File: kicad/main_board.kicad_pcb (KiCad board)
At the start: 2 copper layers, 42 x 67 mm, 55 parts, among them J1 Conn_01x07, J2 Conn_01x07, J3 Conn_01x07, J4 Conn_01x07, J5 Conn_01x07, J6 TYPE-C-31-M-12, J7 TYPE-C-31-M-12, Q1 Q_NPN_BEC, Q2 Q_NPN_BEC, Q3 Q_NPN_BEC, Q4 Q_NPN_BEC, Q5 Q_NPN_BEC, SW1 Reset, SW2 Boot, U1 esp32-s2-wroom, U2 XC6220B331MR, U3 USBLC6-2SC6, U4 USBLC6-2SC6, U5 LMV324, U6 LMV324

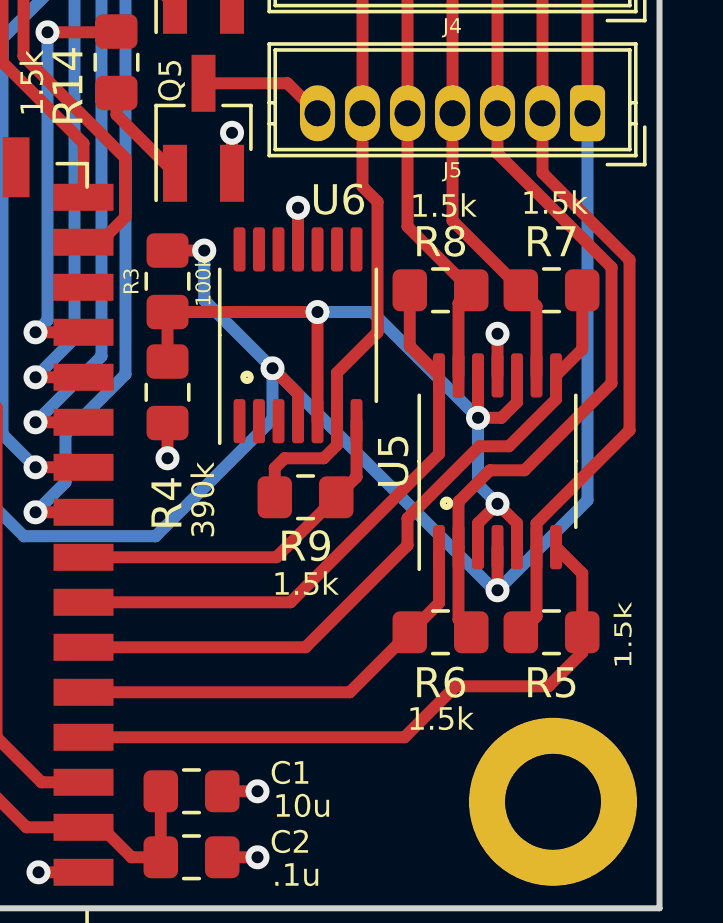
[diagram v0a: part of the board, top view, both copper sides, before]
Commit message: Update the various sensitivity-related resistor values
This updates the transimpedance amplifier resistors to 2k, and adjusts
the LED drive resistors to an appropriate level, from empirical testing.
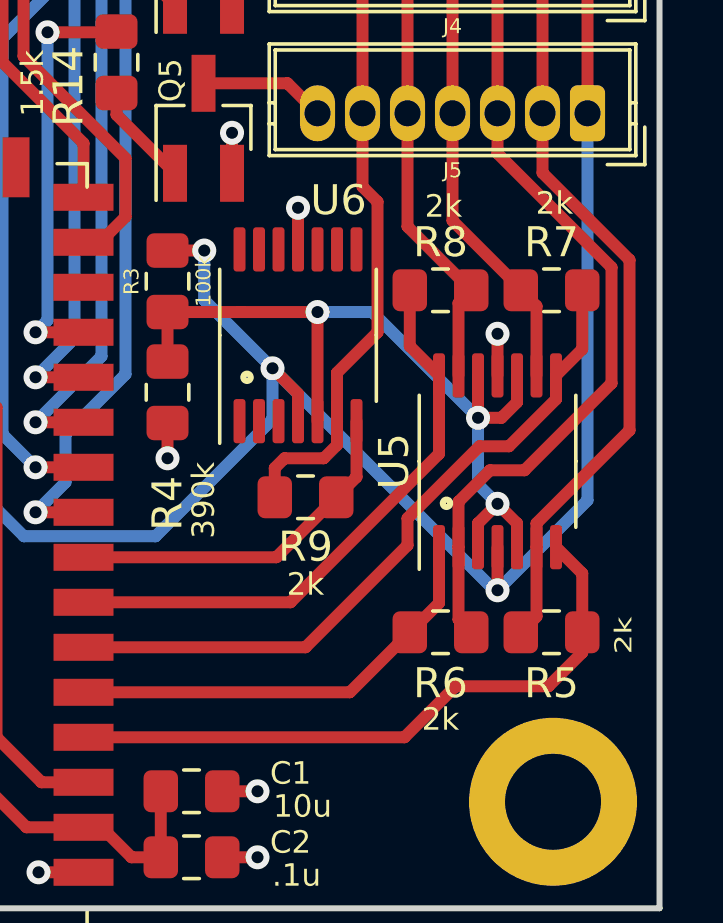
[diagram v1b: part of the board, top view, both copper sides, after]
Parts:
- R5, R6, R7, R8, R9: value 1.5k -> 2k
- U1: value esp32-s2-wroom -> esp32-s2-wrover

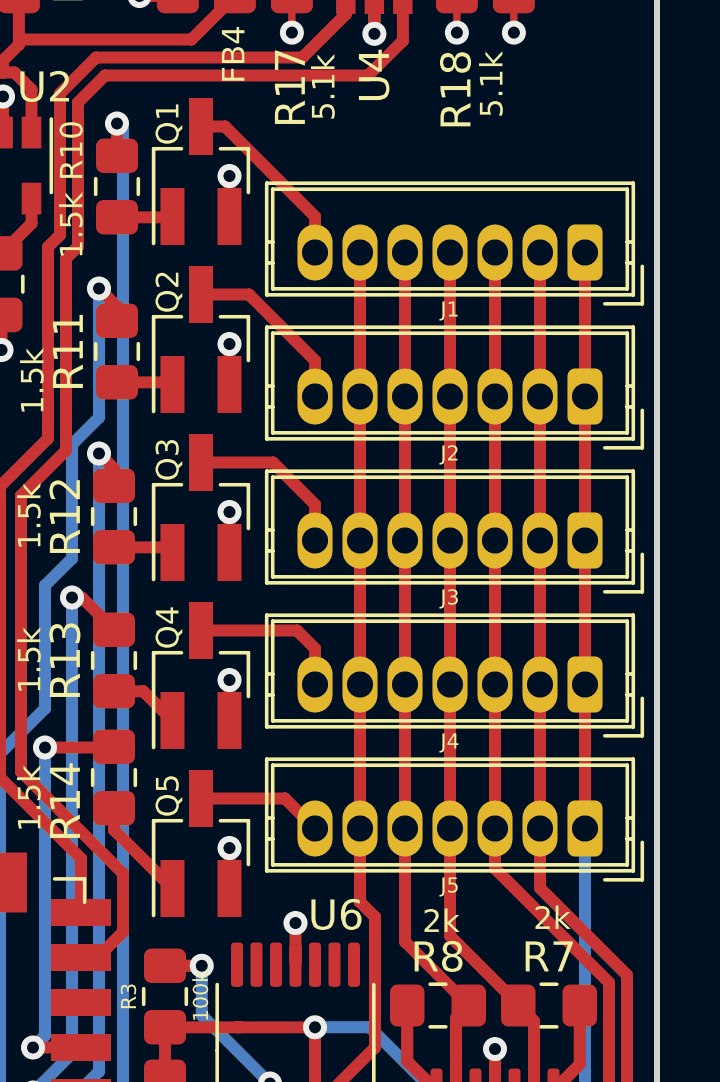
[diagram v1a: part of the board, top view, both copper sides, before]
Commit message: Reverse the cluster connectors on the main board
This reverses the connectors, so the orientation is correct for a normally
wired cable.
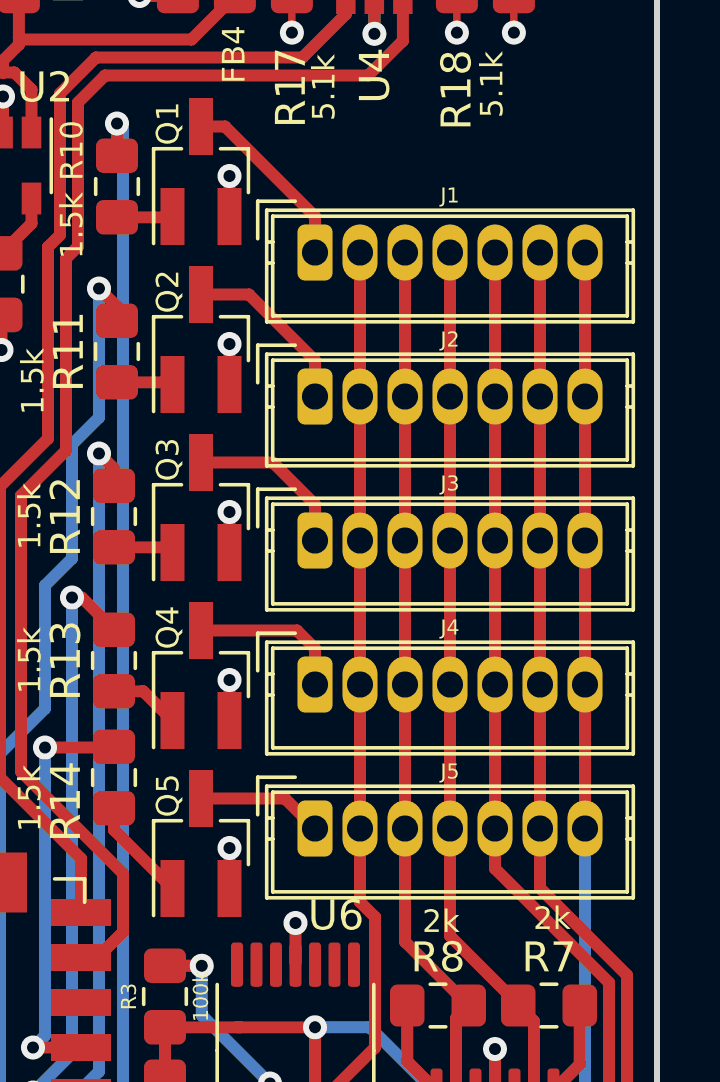
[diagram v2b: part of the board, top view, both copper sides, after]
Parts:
- U1: value esp32-s2-wrover -> esp32-s2-wroom
- moved J1 9.00 mm to (180.6, 54.3), turned to 0 degrees
- moved J2 9.00 mm to (180.6, 59.1), turned to 0 degrees
- moved J3 9.00 mm to (180.6, 63.9), turned to 0 degrees
- moved J4 9.00 mm to (180.6, 68.7), turned to 0 degrees
- moved J5 9.00 mm to (180.6, 73.5), turned to 0 degrees
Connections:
- J1 pad 1: +3V3 -> Net-(J1-Pad1)
- J1 pad 2: /COL1 -> /COL5
- J1 pad 3: /COL2 -> /COL4
- J1 pad 5: /COL4 -> /COL2
- J1 pad 6: /COL5 -> /COL1
- J1 pad 7: Net-(J1-Pad7) -> +3V3
- J2 pad 1: +3V3 -> Net-(J2-Pad1)
- J2 pad 2: /COL1 -> /COL5
- J2 pad 3: /COL2 -> /COL4
- J2 pad 5: /COL4 -> /COL2
- J2 pad 6: /COL5 -> /COL1
- J2 pad 7: Net-(J2-Pad7) -> +3V3
- J3 pad 1: +3V3 -> Net-(J3-Pad1)
- J3 pad 2: /COL1 -> /COL5
- J3 pad 3: /COL2 -> /COL4
- J3 pad 5: /COL4 -> /COL2
- J3 pad 6: /COL5 -> /COL1
- J3 pad 7: Net-(J3-Pad7) -> +3V3
- J4 pad 1: +3V3 -> Net-(J4-Pad1)
- J4 pad 2: /COL1 -> /COL5
- J4 pad 3: /COL2 -> /COL4
- J4 pad 5: /COL4 -> /COL2
- J4 pad 6: /COL5 -> /COL1
- J4 pad 7: Net-(J4-Pad7) -> +3V3
- J5 pad 1: +3V3 -> Net-(J5-Pad1)
- J5 pad 2: /COL1 -> /COL5
- J5 pad 3: /COL2 -> /COL4
- J5 pad 5: /COL4 -> /COL2
- J5 pad 6: /COL5 -> /COL1
- J5 pad 7: Net-(J5-Pad7) -> +3V3
- Q1 pad 3: Net-(J1-Pad7) -> Net-(J1-Pad1)
- Q2 pad 3: Net-(J2-Pad7) -> Net-(J2-Pad1)
- Q3 pad 3: Net-(J3-Pad7) -> Net-(J3-Pad1)
- Q4 pad 3: Net-(J4-Pad7) -> Net-(J4-Pad1)
- Q5 pad 3: Net-(J5-Pad7) -> Net-(J5-Pad1)
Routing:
- net Net-(J2-Pad7): track 6.59 -> 0.00 mm
- net Net-(J2-Pad1): track 0.00 -> 6.59 mm
- net Net-(J1-Pad7): track 6.24 -> 0.00 mm
- net Net-(J1-Pad1): track 0.00 -> 6.24 mm
- net Net-(J3-Pad7): track 5.58 -> 0.00 mm
- net Net-(J3-Pad1): track 0.00 -> 5.58 mm
- net Net-(J4-Pad7): track 5.25 -> 0.00 mm
- net Net-(J4-Pad1): track 0.00 -> 5.25 mm
- net Net-(J5-Pad7): track 4.21 -> 0.00 mm
- net Net-(J5-Pad1): track 0.00 -> 4.21 mm

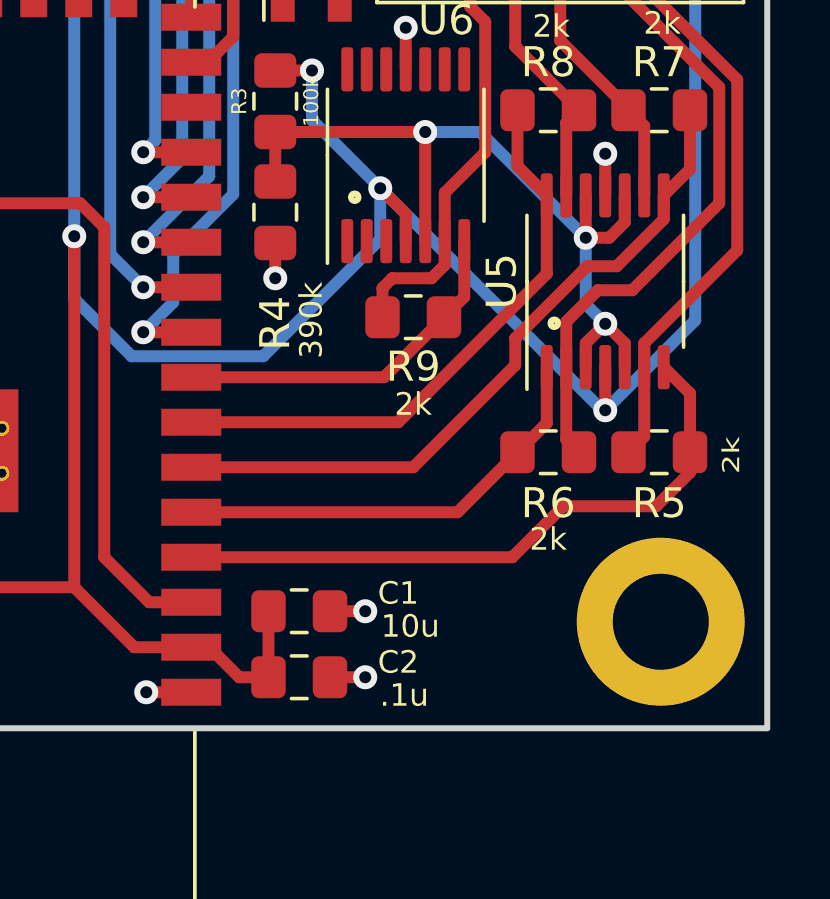
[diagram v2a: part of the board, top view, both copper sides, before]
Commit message: Add a test connector to the main board
This adds an optional jst-zh connector that gives access to the output
signals from the opamps
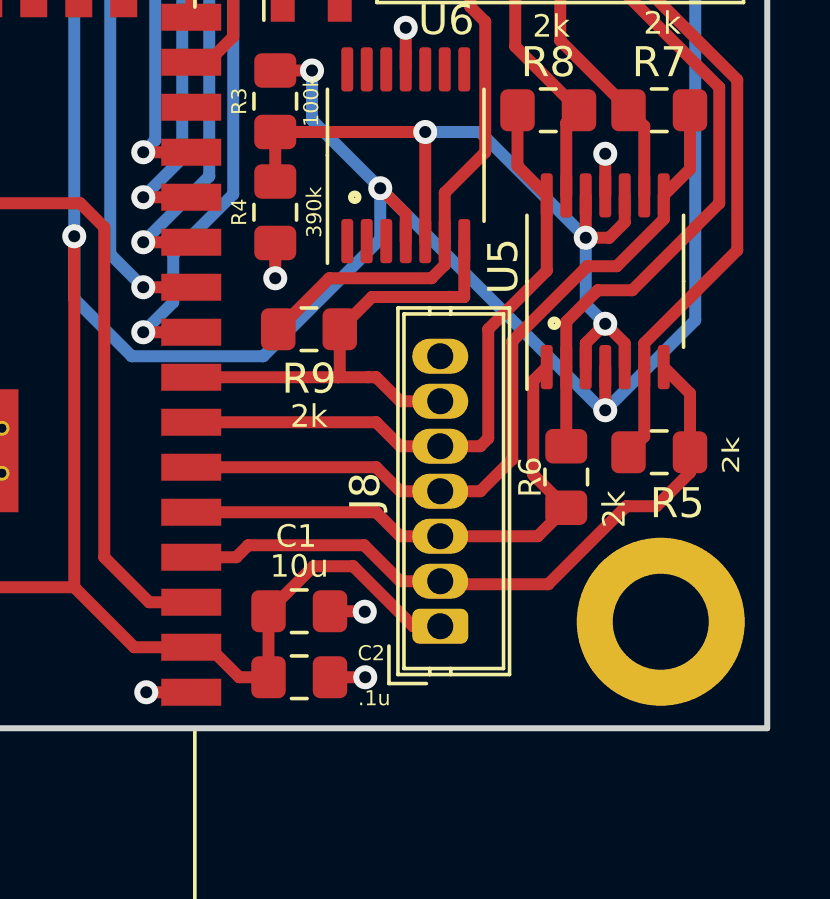
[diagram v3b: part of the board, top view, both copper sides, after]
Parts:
- added J8: Conn_01x07, lalboard:JST_ZH_B7B-ZR_1x07_P1.50mm_Vertical, F.Cu at (181.1, 96.6)
- moved R9 3.50 mm to (176.7, 86.7)
- moved R6 1.02 mm to (185.3, 91.6), turned to 90 degrees
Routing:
- net +3V3: track 151.8 -> 159.0 mm
- net /COL5_AMP: track 12.1 -> 16.7 mm
- net /COL2_AMP: track 14.9 -> 18.7 mm
- net /COL4_AMP: track 19.8 -> 22.8 mm
- net /COL5: track 34.7 -> 37.5 mm
- net /COL3_AMP: track 23.7 -> 26.1 mm
- net /COL1_AMP: track 21.7 -> 22.7 mm

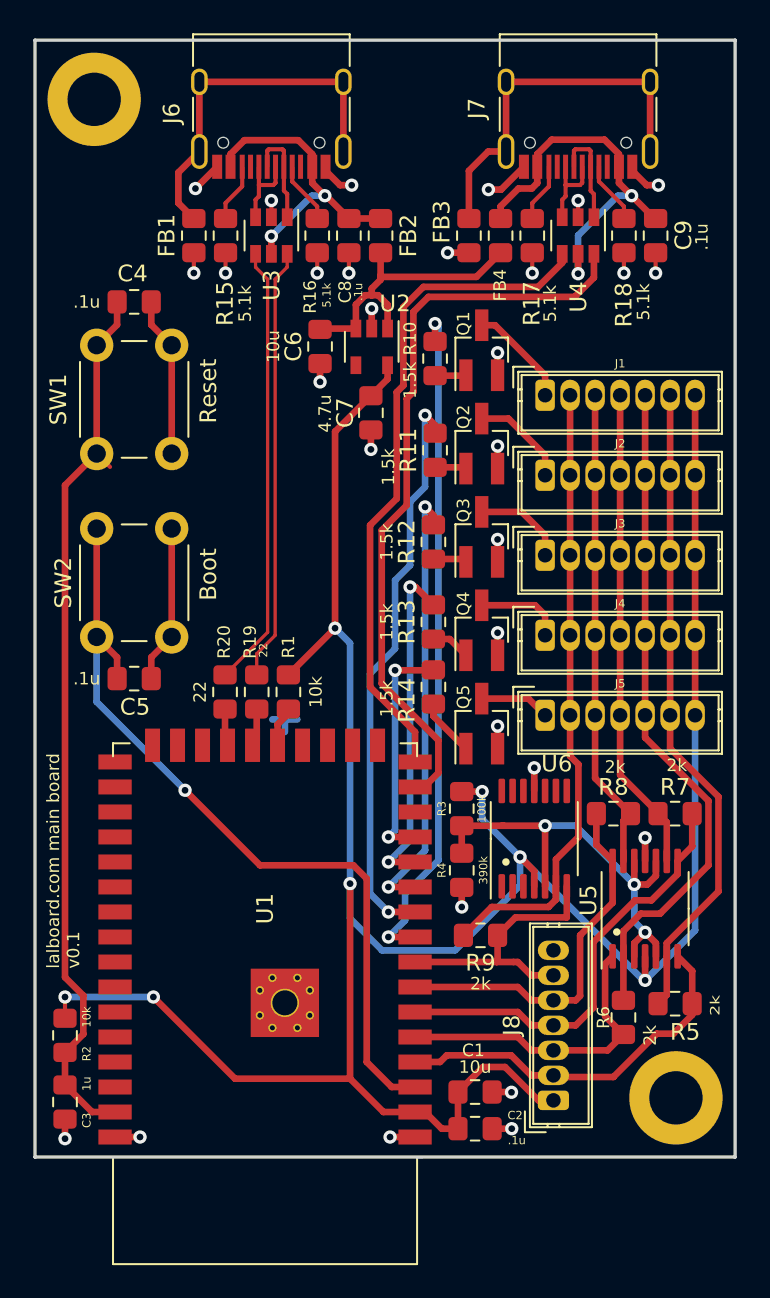
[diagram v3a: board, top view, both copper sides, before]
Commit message: Update the main board for v2.5
This switches from an ESP32 MCU to an RP2040
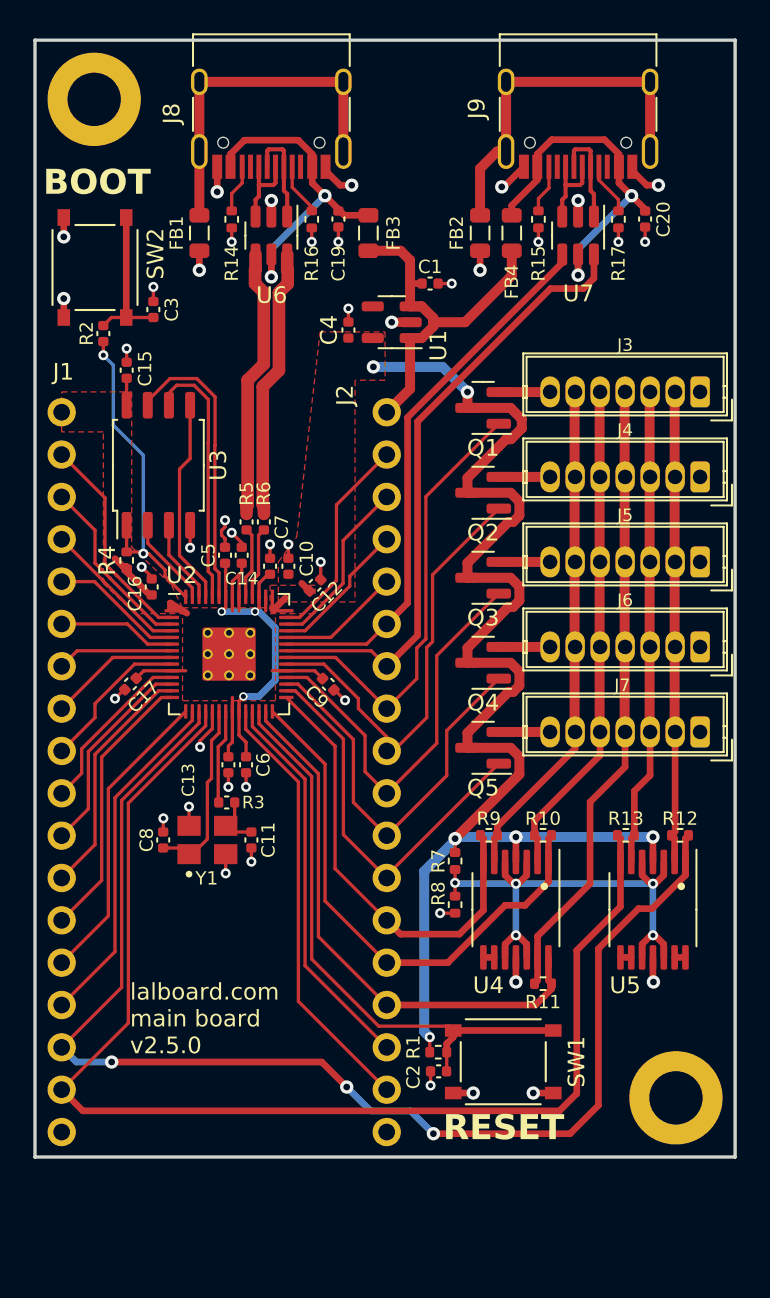
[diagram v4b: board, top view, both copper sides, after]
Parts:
- removed the C1 at (176.4, 96.1)
- removed the C2 at (176.4, 98.3)
- removed the C3 at (151.8, 96.7)
- removed the J8 at (181.1, 96.6)
- removed the R10 at (174.0, 52.1)
- removed the R11 at (174.0, 57.6)
- removed the R12 at (173.9, 63.1)
- removed the R13 at (173.9, 67.9)
- removed the R14 at (173.9, 71.8)
- removed R19, R20: 22, Resistor_SMD:R_0805_2012Metric_Pad1.15x1.40mm_HandSolder
- removed the U1 at (163.8, 85.1)
- added C10: 1u, Capacitor_SMD:C_0402_1005Metric, F.Cu at (165.2, 64.6)
- added C11: 30pF, Capacitor_SMD:C_0402_1005Metric, F.Cu at (163.0, 81.0)
- added C12: 100n, Capacitor_SMD:C_0402_1005Metric, F.Cu at (166.8, 65.7)
- added C13: 100n, Capacitor_SMD:C_0402_1005Metric, F.Cu at (161.6, 76.5)
- added C14: 100n, Capacitor_SMD:C_0402_1005Metric, F.Cu at (162.4, 63.9)
- added C15: 100n, Capacitor_SMD:C_0402_1005Metric, F.Cu at (155.5, 52.8)
- added C16: 100n, Capacitor_SMD:C_0402_1005Metric, F.Cu at (157.0, 65.8)
- added C17: 100n, Capacitor_SMD:C_0402_1005Metric, F.Cu at (155.7, 71.6)
- added C5: 100n, Capacitor_SMD:C_0402_1005Metric, F.Cu at (161.4, 63.9)
- added C6: 100n, Capacitor_SMD:C_0402_1005Metric, F.Cu at (162.7, 76.5)
- added C7: 1u, Capacitor_SMD:C_0402_1005Metric, F.Cu at (164.1, 64.6)
- added C8: 30pF, Capacitor_SMD:C_0402_1005Metric, F.Cu at (157.7, 81.0)
- added C9: 100n, Capacitor_SMD:C_0402_1005Metric, F.Cu at (167.6, 71.6)
- added J6: Conn_01x07, lalboard:JST_ZH_B7B-ZR_1x07_P1.50mm_Vertical, F.Cu at (189.9, 69.4)
- added J7: Conn_01x07, lalboard:JST_ZH_B7B-ZR_1x07_P1.50mm_Vertical, F.Cu at (189.9, 74.5)
- added R3: 1k, Capacitor_SMD:C_0402_1005Metric, F.Cu at (161.5, 78.7)
- added R4: 10k, Resistor_SMD:R_0402_1005Metric, F.Cu at (155.5, 64.2)
- added R5: 27, Capacitor_SMD:C_0402_1005Metric, F.Cu at (162.7, 61.9)
- added R6: 27, Capacitor_SMD:C_0402_1005Metric, F.Cu at (163.7, 61.9)
- added U2: RP2040, lalboard:RP2040-QFN-56, F.Cu at (161.6, 69.8)
- added U3: W25Q128JVS, Package_SO:SOIC-8_5.23x5.23mm_P1.27mm, F.Cu at (157.4, 58.5)
- added Y1: Crystal_GND24, lalboard:OSC_X322516MLB4SI, F.Cu at (160.3, 81.0)
- C1: renamed from C6; footprint Capacitor_SMD:C_0805_2012Metric_Pad1.15x1.40mm_HandSolder -> Capacitor_SMD:C_0402_1005Metric
- C19: renamed from C8; value .1u -> 100n; footprint Capacitor_SMD:C_0805_2012Metric_Pad1.15x1.40mm_HandSolder -> Capacitor_SMD:C_0402_1005Metric
- C2: renamed from C4; value .1u -> 100n; footprint Capacitor_SMD:C_0805_2012Metric_Pad1.15x1.40mm_HandSolder -> Capacitor_SMD:C_0402_1005Metric
- C20: renamed from C9; value .1u -> 100n; footprint Capacitor_SMD:C_0805_2012Metric_Pad1.15x1.40mm_HandSolder -> Capacitor_SMD:C_0402_1005Metric
- C3: renamed from C5; value .1u -> 100n; footprint Capacitor_SMD:C_0805_2012Metric_Pad1.15x1.40mm_HandSolder -> Capacitor_SMD:C_0402_1005Metric
- C4: renamed from C7; footprint Capacitor_SMD:C_0805_2012Metric_Pad1.15x1.40mm_HandSolder -> Capacitor_SMD:C_0402_1005Metric
- FB1, FB4: value ACML-0805-500-T -> CBG201209U500T; footprint Inductor_SMD:L_0805_2012Metric_Pad1.15x1.40mm_HandSolder -> Inductor_SMD:L_0805_2012Metric
- FB2: renamed from FB3; value ACML-0805-500-T -> CBG201209U500T; footprint Inductor_SMD:L_0805_2012Metric_Pad1.15x1.40mm_HandSolder -> Inductor_SMD:L_0805_2012Metric
- FB3: renamed from FB2; value ACML-0805-500-T -> CBG201209U500T; footprint Inductor_SMD:L_0805_2012Metric_Pad1.15x1.40mm_HandSolder -> Inductor_SMD:L_0805_2012Metric
- J1, J2: value Conn_01x07 -> Conn_01x18; footprint lalboard:JST_ZH_B7B-ZR_1x07_P1.50mm_Vertical -> Connector_PinHeader_2.54mm:PinHeader_1x18_P2.54mm_Vertical
- Q1, Q2, Q3, Q4, Q5: value Q_NPN_BEC -> DMG2301L-7; footprint Package_TO_SOT_SMD:SOT-23_Handsoldering -> Package_TO_SOT_SMD:SOT-23
- R1: value 10k -> 1.5k; footprint Resistor_SMD:R_0805_2012Metric_Pad1.15x1.40mm_HandSolder -> Resistor_SMD:R_0402_1005Metric
- R10: renamed from R6; footprint Resistor_SMD:R_0805_2012Metric_Pad1.15x1.40mm_HandSolder -> Resistor_SMD:R_0402_1005Metric
- R11: renamed from R7; footprint Resistor_SMD:R_0805_2012Metric_Pad1.15x1.40mm_HandSolder -> Resistor_SMD:R_0402_1005Metric
- R12: renamed from R8; footprint Resistor_SMD:R_0805_2012Metric_Pad1.15x1.40mm_HandSolder -> Resistor_SMD:R_0402_1005Metric
- R13: renamed from R9; footprint Resistor_SMD:R_0805_2012Metric_Pad1.15x1.40mm_HandSolder -> Resistor_SMD:R_0402_1005Metric
- R14: renamed from R15; footprint Resistor_SMD:R_0805_2012Metric_Pad1.15x1.40mm_HandSolder -> Resistor_SMD:R_0402_1005Metric
- R15: renamed from R17; footprint Resistor_SMD:R_0805_2012Metric_Pad1.15x1.40mm_HandSolder -> Resistor_SMD:R_0402_1005Metric
- R16: footprint Resistor_SMD:R_0805_2012Metric_Pad1.15x1.40mm_HandSolder -> Resistor_SMD:R_0402_1005Metric
- R17: renamed from R18; footprint Resistor_SMD:R_0805_2012Metric_Pad1.15x1.40mm_HandSolder -> Resistor_SMD:R_0402_1005Metric
- R2: value 10k -> 1k; footprint Resistor_SMD:R_0805_2012Metric_Pad1.15x1.40mm_HandSolder -> Capacitor_SMD:C_0402_1005Metric
- R7: renamed from R3; footprint Resistor_SMD:R_0805_2012Metric_Pad1.15x1.40mm_HandSolder -> Resistor_SMD:R_0402_1005Metric
- R8: renamed from R4; footprint Resistor_SMD:R_0805_2012Metric_Pad1.15x1.40mm_HandSolder -> Resistor_SMD:R_0402_1005Metric
- R9: renamed from R5; footprint Resistor_SMD:R_0805_2012Metric_Pad1.15x1.40mm_HandSolder -> Resistor_SMD:R_0402_1005Metric
- SW1, SW2: footprint Button_Switch_THT:SW_PUSH_6mm_H5mm -> lalboard:SW_TS-1187A-B-A-B
- U4: renamed from U5; value LMV324 -> COS724
- U5: renamed from U6; value LMV324 -> COS724
- moved C2 49.6 mm to (174.2, 94.9), turned to 0 degrees
- moved SW1 43.9 mm to (178.1, 94.3), turned to 0 degrees
- moved R2 42.2 mm to (154.1, 50.6)
- moved J1 29.0 mm to (151.6, 55.3)
- moved R1 23.4 mm to (174.2, 93.7), turned to 0 degrees
- moved C3 22.2 mm to (157.1, 49.2), turned to 90 degrees
- moved SW2 22.2 mm to (153.6, 46.6), turned to -90 degrees
- moved R9 15.1 mm to (177.2, 80.7), turned to 0 degrees
- moved J3 13.5 mm to (189.9, 54.1), turned to 180 degrees
- moved J4 13.3 mm to (189.9, 59.2), turned to 180 degrees
- moved J5 13.1 mm to (189.9, 64.3), turned to 180 degrees
- moved R11 12.9 mm to (180.5, 89.6)
- moved R10 11.9 mm to (180.5, 80.7), turned to 180 degrees
- moved R13 10.6 mm to (185.4, 80.7), turned to 0 degrees
- moved J2 10.2 mm to (171.1, 55.3)
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- renumbered J6 to J8, J7 to J9, U2 to U1, U3 to U6, U4 to U7
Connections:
- C2 pad 2: /CHIP_PU -> /RUN
- C3 pad 1: /GPIO_0 -> Net-(C3-Pad1)
- C4 pad 1: +3V3 -> +3.3V
- J1 pad 1: Net-(J1-Pad1) -> +3.3V
- J1 pad 2: /COL5 -> /GPIO0
- J1 pad 3: /COL4 -> /GPIO1
- J1 pad 4: /COL3 -> /GPIO2
- J1 pad 5: /COL2 -> /GPIO3
- J1 pad 6: /COL1 -> /GPIO4
- J1 pad 7: +3V3 -> /GPIO5
- J2 pad 1: Net-(J2-Pad1) -> +5V
- J2 pad 2: /COL5 -> /GPIO29_ADC3
- J2 pad 3: /COL4 -> /GPIO28_ADC2
- J2 pad 4: /COL3 -> /GPIO27_ADC1
- J2 pad 5: /COL2 -> /GPIO26_ADC0
- J2 pad 6: /COL1 -> /U1RX
- J2 pad 7: +3V3 -> /U1TX
- J3 pad 1: Net-(J3-Pad1) -> GND
- J3 pad 7: +3V3 -> Net-(J3-Pin_7)
- J4 pad 1: Net-(J4-Pad1) -> GND
- J4 pad 7: +3V3 -> Net-(J4-Pin_7)
- J5 pad 1: Net-(J5-Pad1) -> GND
- J5 pad 7: +3V3 -> Net-(J5-Pin_7)
- J8 pad A8: Net-(J6-PadA8) -> unconnected-(J8-SBU1-PadA8)
- J8 pad B8: Net-(J6-PadB8) -> unconnected-(J8-SBU2-PadB8)
- J9 pad A6: /U1TX_raw -> /U1RX_raw
- J9 pad A7: /U1RX_raw -> /U1TX_raw
- J9 pad A8: Net-(J7-PadA8) -> unconnected-(J9-SBU1-PadA8)
- J9 pad B6: /U1TX_raw -> /U1RX_raw
- J9 pad B7: /U1RX_raw -> /U1TX_raw
- J9 pad B8: Net-(J7-PadB8) -> unconnected-(J9-SBU2-PadB8)
- Q1 pad 1: Net-(Q1-Pad1) -> /ROW5
- Q1 pad 2: GND -> Net-(J3-Pin_7)
- Q1 pad 3: Net-(J1-Pad1) -> +3.3V
- Q2 pad 1: Net-(Q2-Pad1) -> /ROW4
- Q2 pad 2: GND -> Net-(J4-Pin_7)
- Q2 pad 3: Net-(J2-Pad1) -> +3.3V
- Q3 pad 1: Net-(Q3-Pad1) -> /ROW3
- Q3 pad 2: GND -> Net-(J5-Pin_7)
- Q3 pad 3: Net-(J3-Pad1) -> +3.3V
- Q4 pad 1: Net-(Q4-Pad1) -> /ROW2
- Q4 pad 2: GND -> Net-(J6-Pin_7)
- Q4 pad 3: Net-(J4-Pad1) -> +3.3V
- Q5 pad 1: Net-(Q5-Pad1) -> /ROW1
- Q5 pad 2: GND -> Net-(J7-Pin_7)
- Q5 pad 3: Net-(J5-Pad1) -> +3.3V
- R1 pad 1: Net-(R1-Pad1) -> +3.3V
- R1 pad 2: +3V3 -> /RUN
- R12 pad 1: /COL4_AMP -> /COL5_AMP
- R12 pad 2: /COL4 -> /COL5
- R13 pad 1: /COL5_AMP -> /COL4_AMP
- R13 pad 2: /COL5 -> /COL4
- R2 pad 1: +3V3 -> Net-(C3-Pad1)
- R2 pad 2: /CHIP_PU -> /QSPI_SS
- R7 pad 1: +3V3 -> +3.3V
- SW1 pad 1: /CHIP_PU -> /RUN
- SW2 pad 1: /GPIO_0 -> Net-(C3-Pad1)
- U1 pad 4: Net-(U2-Pad4) -> unconnected-(U1-NC-Pad4)
- U1 pad 5: +3V3 -> +3.3V
- U4 pad 13: /COL4 -> /COL3
- U4 pad 14: /COL4_AMP -> /COL3_AMP
- U4 pad 4: +3V3 -> +3.3V
- U4 pad 8: /COL3_AMP -> Net-(U4C--)
- U4 pad 9: /COL3 -> Net-(U4C--)
- U5 pad 1: (no net) -> /COL5_AMP
- U5 pad 10: (no net) -> /AMP_REF
- U5 pad 12: (no net) -> /AMP_REF
- U5 pad 13: (no net) -> Net-(U5D--)
- U5 pad 14: (no net) -> Net-(U5D--)
- U5 pad 2: (no net) -> /COL5
- U5 pad 3: (no net) -> /AMP_REF
- U5 pad 4: +3V3 -> +3.3V
- U5 pad 6: /COL5 -> /COL4
- U5 pad 7: /COL5_AMP -> /COL4_AMP
- U5 pad 8: (no net) -> Net-(U5C--)
- U5 pad 9: (no net) -> Net-(U5C--)
- U7 pad 1: /U1RX_raw -> /U1TX_raw
- U7 pad 3: /U1TX_raw -> /U1RX_raw
- U7 pad 4: /U1TX -> /U1RX
- U7 pad 6: /U1RX -> /U1TX
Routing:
- net +3V3: track 159.0 -> 0.00 mm, vias 7 -> 0
- net +3.3V: track 0.00 -> 110.9 mm, vias 0 -> 6
- net /COL5_AMP: track 16.7 -> 77.5 mm, vias 0 -> 3
- net /CHIP_PU: track 54.0 -> 0.00 mm
- net /COL4_AMP: track 22.8 -> 74.8 mm
- net /GPIO_0: track 48.5 -> 0.00 mm, vias 1 -> 0
- net /RUN: track 0.00 -> 35.0 mm
- net /SWCLK: track 0.00 -> 26.2 mm
- net /SWD: track 0.00 -> 23.5 mm
- net /GPIO13: track 0.00 -> 20.9 mm
- net /QSPI_SS: track 0.00 -> 20.4 mm, vias 0 -> 2
- net +1V1: track 0.00 -> 18.7 mm, vias 0 -> 3
- net /GPIO12: track 0.00 -> 18.2 mm
- net /QSPI_SD3: track 0.00 -> 17.4 mm
- net /GPIO11: track 0.00 -> 16.5 mm
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- added copper zone on F.Cu, net +3.3V
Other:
- net class Default removed
- board text added: "BOOT"
- board text added: "RESET"
- board text added: "lalboard.com main board v2.5.0"
- board text removed: "lalboard.com main board v0.1"

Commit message: Add production files for the PCBs
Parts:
- R10, R11, R12, R13, R9: footprint Resistor_SMD:R_0402_1005Metric -> Resistor_SMD:R_0402_1005Metric_Pad0.72x0.64mm_HandSolder
- moved R7 0.30 mm to (175.2, 81.9)
- moved R8 0.30 mm to (175.2, 84.6)
